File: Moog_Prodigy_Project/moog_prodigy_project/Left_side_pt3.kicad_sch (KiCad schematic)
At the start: 68 parts, among them J1 P2-3, J2 P2-4, J3 P2-2, J4 P2-1, J5 P2-1, SW6 Switch_1x3, SW7 Switch_4x4, SW8 SW_Slide_DPDT_3x3, U10 NE5532, U11 OPA234, U12 OPA134, U13 NE5532, U14 OPA134, U9 NE5532

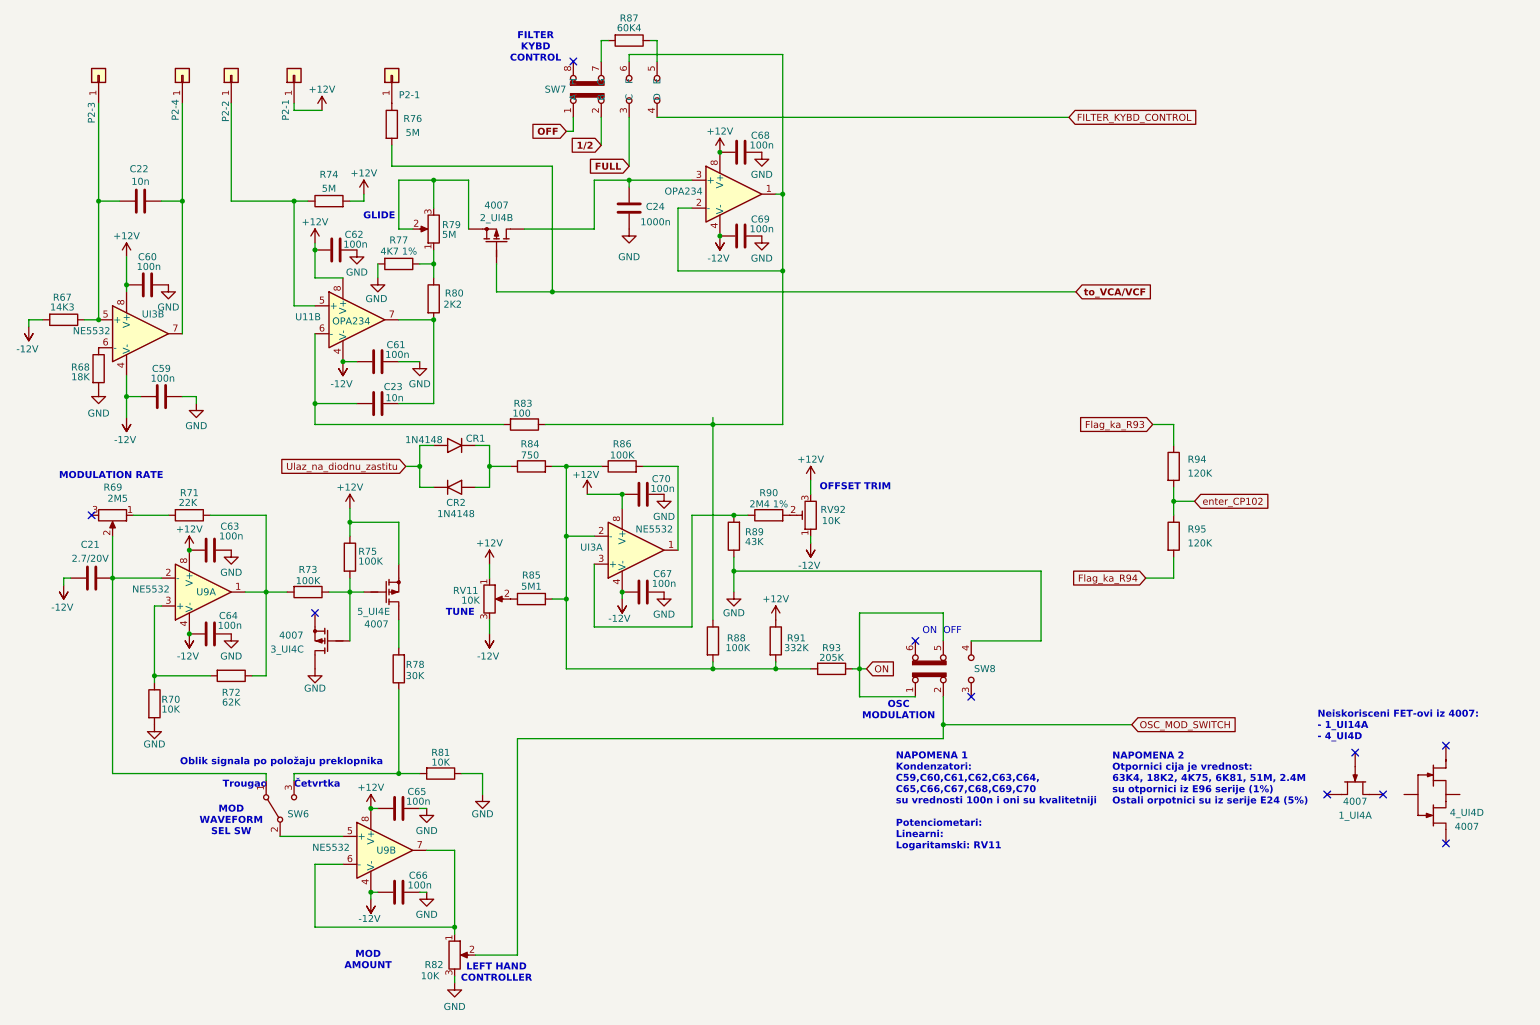
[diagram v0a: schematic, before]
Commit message: Moog prodigy fix 3
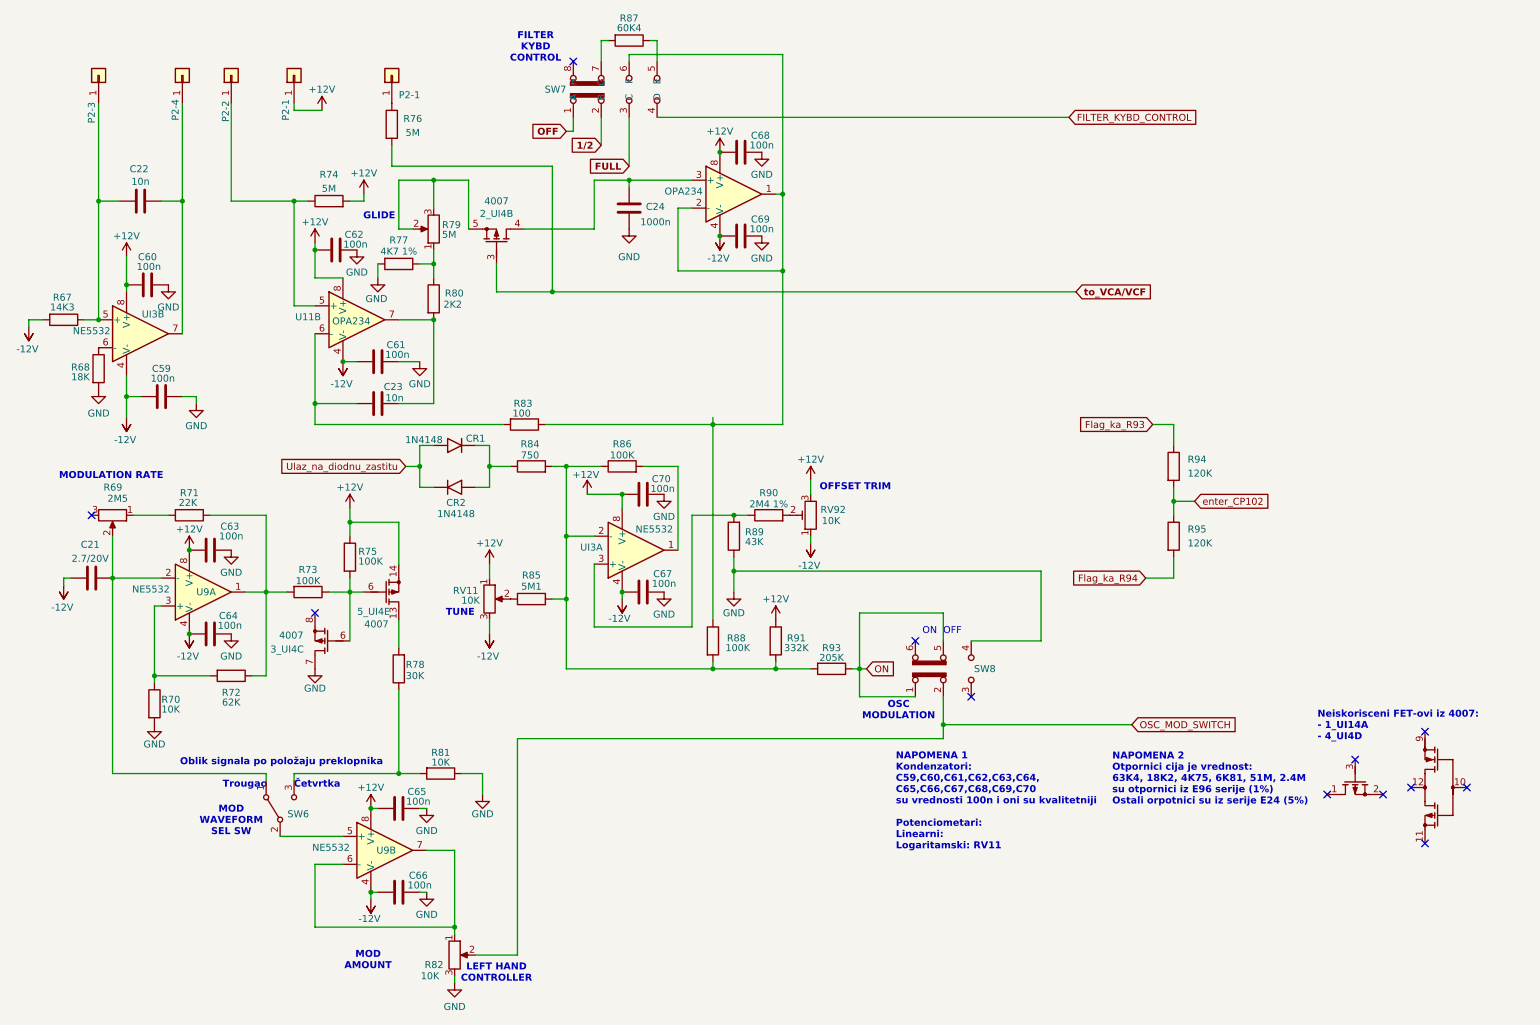
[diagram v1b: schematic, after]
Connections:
- net +12V: now also 5_UI4.14; no longer 5_UI4.
- net GND: now also 3_UI4.7; no longer 3_UI4.
- net to_VCA/VCF: now also 2_UI4.3; no longer 2_UI4.
- net at R73.1, R75.2: now also 3_UI4.6, 5_UI4.6; no longer 3_UI4., 5_UI4.
- net at C24.2, U11.3 (+): now also 2_UI4.4; no longer 2_UI4.
- net at R78.2: now also 5_UI4.13; no longer 5_UI4.
- net at R79.2, R79.3: now also 2_UI4.5; no longer 2_UI4.
- no-connect marks 10 -> 12
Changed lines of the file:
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@@
 	)
 	(no_connect
-		(at 276.86 163.83)
+		(at 273.05 163.83)
 	)
 	(no_connect
@@
 	)
 	(no_connect
-		(at 276.86 146.05)
+		(at 280.67 153.67)
+	)
+	(no_connect
+		(at 273.05 143.51)
 	)
 	(no_connect
@@
 	)
 	(no_connect
-		(at 260.35 147.32)
+		(at 260.35 148.59)
+	)
+	(no_connect
+		(at 270.51 153.67)
 	)
 	(wire
@@
 		(dnp no)
 		(property "Reference" "2_UI4"
-			(at 104.14 50.038 90)
+			(at 104.14 49.276 90)
 			(effects
 				(font
@@
 		)
 		(property "Value" "4007"
-			(at 104.14 47.752 90)
+			(at 104.14 46.99 90)
 			(effects
 				(font
@@
 		(pin ""
 		)
-		(pin ""
+		(pin "5"
 		)
 		(pin ""
 		)
-		(pin ""
+		(pin "3"
 		)
 		(pin ""
 		)
-		(pin ""
+		(pin "4"
 		)
 		(instances
@@
 		(pin ""
 		)
-		(pin ""
+		(pin "6"
 		)
 		(pin ""
@@
 		(pin ""
 		)
-		(pin ""
+		(pin "8"
 		)
 		(pin ""
 		)
-		(pin ""
+		(pin "7"
 		)
 		(pin ""
@@
 		(lib_name "4007_Novi_1")
 		(lib_id "Transistor_FET:4007_Novi")
-		(at 260.35 154.94 90)
+		(at 260.35 163.83 90)
 		(unit 1)
 		(exclude_from_sim no)
@@
 		(fields_autoplaced yes)
 		(property "Reference" "1_UI4"
-			(at 260.35 158.75 90)
+			(at 260.35 167.64 90)
 			(effects
 				(font
 					(size 1.27 1.27)
 				)
+				(hide yes)
 			)
 		)
 		(property "Value" "4007"
-			(at 260.35 156.21 90)
+			(at 260.35 165.1 90)
 			(effects
 				(font
 					(size 1.27 1.27)
 				)
+				(hide yes)
 			)
 		)
 		(property "Footprint" "Package_DIP:DIP-14_W7.62mm_Socket"
-			(at 260.35 154.94 0)
+			(at 260.35 163.83 0)
 			(effects
 				(font
@@
 		)
 		(property "Datasheet" ""
-			(at 260.35 154.94 0)
+			(at 260.35 163.83 0)
 			(effects
 				(font
@@
 		)
 		(property "Description" ""
-			(at 260.35 154.94 0)
+			(at 260.35 163.83 0)
 			(effects
 				(font
@@
 		(pin ""
 		)
-		(pin ""
+		(pin "3"
 		)
-		(pin ""
+		(pin "2"
 		)
-		(pin ""
+		(pin "1"
 		)
 		(pin ""
@@
 		(pin ""
 		)
-		(pin ""
+		(pin "14"
 		)
 		(pin ""
@@
 		(pin ""
 		)
-		(pin ""
+		(pin "13"
 		)
 		(pin ""
@@
 		(pin ""
 		)
-		(pin ""
+		(pin "6"
 		)
 		(pin ""
@@
 		(lib_name "4007_Novi_2")
 		(lib_id "Transistor_FET:4007_Novi")
-		(at 276.86 158.75 180)
+		(at 274.32 156.21 180)
 		(unit 4)
 		(exclude_from_sim no)
@@
 		(dnp no)
 		(property "Reference" "4_UI4"
-			(at 280.67 158.242 0)
+			(at 281.686 157.734 0)
 			(effects
 				(font
 					(size 1.27 1.27)
 				)
+				(hide yes)
 			)
 		)
 		(property "Value" "4007"
-			(at 280.67 160.782 0)
+			(at 278.13 158.242 0)
 			(effects
 				(font
 					(size 1.27 1.27)
 				)
+				(hide yes)
 			)
 		)
 		(property "Footprint" "Package_DIP:DIP-14_W7.62mm_Socket"
-			(at 276.86 158.75 0)
+			(at 280.67 153.67 0)
 			(effects
 				(font
@@
 		)
 		(property "Datasheet" ""
-			(at 276.86 158.75 0)
+			(at 274.32 156.21 0)
 			(effects
 				(font
@@
 		)
 		(property "Description" ""
-			(at 276.86 158.75 0)
+			(at 274.32 156.21 0)
 			(effects
 				(font
@@
 		(pin ""
 		)
-		(pin ""
+		(pin "10"
 		)
 		(pin ""
@@
 		(pin ""
 		)
-		(pin ""
+		(pin "11"
 		)
-		(pin ""
+		(pin "9"
 		)
-		(pin ""
+		(pin "12"
 		)
 		(instances

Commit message: treba mi da preraspodelim CA 3046
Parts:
- 2_UI4, 3_UI4, 5_UI4: value 4007 -> MC14007UBCP
- renumbered CR2 to D8, CR1 to D9
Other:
- note added: "Neiskorisceni FET-ovi iz MC14007UBCP - 1_UI14A - 4_UI4D"
- note removed: "Neiskorisceni FET-ovi iz 4007: - 1_UI14A - 4_UI4D"
- moved on the sheet: C60, R78

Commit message: 04.07.2026 Dodati tolerancije, E94, prosiriti spisak
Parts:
- U10: value NE5532 -> ~
- UI3: footprint NE5532AP:DIP794W45P254L1016H508Q8 -> Package_DIP:DIP-8_W7.62mm
- renumbered RV11 to RV11_LOG
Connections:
- net Flag_ka_R93 renamed Flag_to_R93
- net Flag_ka_R94 renamed Flag_to_R94
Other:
- note added: "32-key keyboard matrix generating scaled control voltages for VCO and filter tracking"
- note added: "NAPOMENA 1 Kondenzatori: C59,C60,C61,C62,C63,C64, C65,C66,C67,C68,C69,C70 su vrednosti 100n i oni su kvalitetniji"
- note added: "Not used FETs from MC14007UBCP - 1_UI14A - 4_UI4D"
- note added: "SIGNAL SHAPE TRIANGLE SQUARE"
- note removed: "NAPOMENA 1 Kondenzatori: C59,C60,C61,C62,C63,C64, C65,C66,C67,C68,C69,C70 su vrednosti 100n i oni su kvalitetniji Potenciometari: Linearni: Logaritamski: RV11"
- note removed: "Neiskorisceni FET-ovi iz MC14007UBCP - 1_UI14A - 4_UI4D"
- note removed: "Oblik signala po položaju preklopnika Trougao Četvrtka"
- moved on the sheet: 2_UI4B, 3_UI4C, C59, C63, C64, R75, R78, R83, R85, R86, R89, R90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

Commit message: 07.06.2026 fix 3
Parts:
- added R121, R122, R124, R125, R140: 2K, Resistor_THT:R_Axial_DIN0207_L6.3mm_D2.5mm_P7.62mm_Horizontal, symbol Device:R
- added R123: 100, Resistor_THT:R_Axial_DIN0207_L6.3mm_D2.5mm_P7.62mm_Horizontal, symbol Device:R
- R68: value 18K -> 17K8
- R71: value 22K -> 20K
- R72: value 62K -> 61K9
- R74, R79: value 5M -> 5M1
- R77: value 4K7 1% -> 4K75 1%
- R78: value 30K -> 28K
- R89: value 43K -> 43K2
- R90: value 2M4 1% -> 2M43
- R94, R95: value 120K -> 118K
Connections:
- net Flag_to_R94: now also R140.2; no longer R95.2
- net GND: now also R121.2; no longer R68.2
- net enter_CP102: now also R125.2; no longer R94.2
- net at R73.2, U9.1: now also R122.1, R123.1; no longer R71.1, R72.1
- net at R84.2, R85.2, R86.1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: now also UI3.3 (+); no longer UI3.2 (-)
- net at R81.2, SW6.3 (C): now also R124.1; no longer R78.1
- net at R89.2, R90.1: now also UI3.2 (-); no longer UI3.3 (+)
- net at C21.1, R69.2, SW6.1 (A): now also U9.3 (+); no longer U9.2 (-)
- net at R70.1, R72.2: now also U9.2 (-); no longer U9.3 (+)
- new net: R125.1, R94.2
- new net: R140.1, R95.2
- new net: R122.2, R71.1
- new net: R121.1, R68.2
- new net: R123.2, R72.1
- new net: R124.2, R78.1
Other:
- note removed: "NAPOMENA 2 Otpornici cija je vrednost: 63K4, 18K2, 4K75, 6K81, 51M, 2.4M su otpornici iz E96 serije (1%) Ostali orpotnici su iz serije E24 (5%)"
- moved on the sheet: R71, R72, R78, R85, R94, R95, RV11_LOG

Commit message: CA3046 nova schema
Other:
- note added: "NAPOMENA 1 Kondenzatori: C21,C24,C59,C60,C61,C62,C63,C64, C65,C66,C67,C68,C69,C70 su vrednosti 100n i oni su kvalitetniji"
- note removed: "NAPOMENA 1 Kondenzatori: C59,C60,C61,C62,C63,C64, C65,C66,C67,C68,C69,C70 su vrednosti 100n i oni su kvalitetniji"
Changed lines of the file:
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@@
 		)
 	)
-	(text "NAPOMENA 1\nKondenzatori:\nC59,C60,C61,C62,C63,C64,\nC65,C66,C67,C68,C69,C70\nsu vrednosti 100n i oni su kvalitetniji"
+	(text "NAPOMENA 1\nKondenzatori:\nC21,C24,C59,C60,C61,C62,C63,C64,\nC65,C66,C67,C68,C69,C70\nsu vrednosti 100n i oni su kvalitetniji"
 		(exclude_from_sim no)
 		(at 176.784 156.21 0)

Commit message: 08.07.2026 fix
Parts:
- removed C24: 1000n, Capacitor_THT:C_Disc_D3.8mm_W2.6mm_P2.50mm, symbol Device:C
- removed R121, R122, R124, R125, R140: 2K, Resistor_THT:R_Axial_DIN0207_L6.3mm_D2.5mm_P7.62mm_Horizontal, symbol Device:R
- removed R123: 100, Resistor_THT:R_Axial_DIN0207_L6.3mm_D2.5mm_P7.62mm_Horizontal, symbol Device:R
- added C24: 1u/25V, Capacitor_THT:CP_Radial_D5.0mm_P2.50mm, symbol elektrolitski:elektrolit
- C21: value 2.7/20V -> 2u7/25V
- R68: value 17K8 -> 18K 5%
- R71: value 20K -> 22K 10%
- R72: value 61K9 -> 62K 5%
- R78: value 28K -> 30K 5%
- R84: value 750 -> 750K
- R94, R95: value 118K -> 120K 5%
- RV11: renamed from RV11_LOG; value 10K -> 10K LOG
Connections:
- net enter_CP102 is gone; now on net Input to C39: R95.1
- net GND: now also R68.2, C24.
- net Input to C39: now reaches R94.2
- net Flag to R94: now reaches R95.2
- net at R71.1: now also R72.1, R73.2, U9.1
- net at 2_UI4.4, U11.3 (+): now also C24.
- net at R78.1: now also R81.2, SW6.3 (C)
- net Flag to R87: now reaches R86.2, UI3.1
- net 1/2: no longer names the net of SW7.2
- net FILTER_KYBD_CONTROL renamed FILTER KYBD CONTROL
- net FULL: no longer names the net of SW7.3
- net OFF: no longer names the net of SW7.1
- net OSC_MOD_SWITCH renamed OSC MOD SWITCH
- net Ulaz_na_diodnu_zastitu renamed Input to diode protection
- net to_VCA/VCF renamed Input to VCA/VCF
- no-connect marks 12 -> 15
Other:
- note added: "OFF 1/2 FULL"
- note added: "PP"
- note removed: "NAPOMENA 1 Kondenzatori: C21,C24,C59,C60,C61,C62,C63,C64, C65,C66,C67,C68,C69,C70 su vrednosti 100n i oni su kvalitetniji"
- moved on the sheet: C22, C60, R68, R71, R72, R78, R83, R84, R85, R95, RV11

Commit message: Finalni deo seme, prelaz na PCB
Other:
- note added: "*GENERAL NOTE* Resistor values that are not explicitly specified are selected from the E96 value series with a tolerance of ±1%."
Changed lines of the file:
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@@
 		)
 	)
+	(text "*GENERAL NOTE*\nResistor values that are not explicitly specified\nare selected from the E96 value series with a \ntolerance of ±1%."
+		(exclude_from_sim no)
+		(at 176.784 161.036 0)
+		(effects
+			(font
+				(size 1.27 1.27)
+				(thickness 0.254)
+				(bold yes)
+			)
+			(justify left)
+		)
+	)
 	(text "ON  OFF "
 		(exclude_from_sim no)
@@
 	)
 	(symbol
+		(lib_name "elektrolit_1")
+		(lib_id "elektrolitski:elektrolit")
+		(at 132.08 46.99 0)
+		(unit 1)
+		(exclude_from_sim no)
+		(in_bom yes)
+		(on_board yes)
+		(dnp no)
+		(property "Reference" "C24"
+			(at 128.778 46.99 0)
+			(effects
+				(font
+					(size 1.27 1.27)
+				)
+				(justify right)
+			)
+		)
+		(property "Value" "1u/25V"
+			(at 131.826 49.53 0)
+			(effects
+				(font
+					(size 1.27 1.27)
+				)
+				(justify right)
+			)
+		)
+		(property "Footprint" "Capacitor_THT:CP_Radial_D5.0mm_P2.50mm"
+			(at 132.08 58.42 0)
+			(effects
+				(font
+					(size 1.27 1.27)
+				)
+				(hide yes)
+			)
+		)
+		(property "Datasheet" ""
+			(at 131.826 46.99 0)
+			(effects
+				(font
+					(size 1.27 1.27)
+				)
+				(hide yes)
+			)
+		)
+		(property "Description" ""
+			(at 132.08 46.99 0)
+			(effects
+				(font
+					(size 1.27 1.27)
+				)
+			)
+		)
+		(property "Rated Voltage" "25V"
+			(at 128.524 51.308 0)
+			(effects
+				(font
+					(size 1.27 1.27)
+				)
+				(hide yes)
+			)
+		)
+		(pin ""
+		)
+		(pin ""
+		)
+		(instances
+			(project "moog_prodigy_project"
+				(path "/db469bdb-b6c3-4a16-9199-d4e6b8d556e8/e17106b4-4b3e-4539-a6cd-812d9801e405"
+					(reference "C24")
+					(unit 1)
+				)
+			)
+		)
+	)
+	(symbol
 		(lib_id "Device:R")
 		(at 165.1 132.08 270)
@@
 				)
 			)
-		)
-	)
-	(symbol
-		(lib_name "elektrolit_1")
-		(lib_id "elektrolitski:elektrolit")
-		(at 132.08 46.99 0)
-		(unit 1)
-		(exclude_from_sim no)
-		(in_bom yes)
-		(on_board yes)
-		(dnp no)
-		(property "Reference" "C24"
-			(at 128.778 46.99 0)
-			(effects
-				(font
-					(size 1.27 1.27)
-				)
-				(justify right)
-			)
-		)
-		(property "Value" "1u/25V"
-			(at 131.826 49.53 0)
-			(effects
-				(font
-					(size 1.27 1.27)
-				)
-				(justify right)
-			)
-		)
-		(property "Footprint" "Capacitor_THT:CP_Radial_D5.0mm_P2.50mm"
-			(at 132.08 58.42 0)
-			(effects
-				(font
-					(size 1.27 1.27)
-				)
-				(hide yes)
-			)
-		)
-		(property "Datasheet" ""
-			(at 131.826 46.99 0)
-			(effects
-				(font
-					(size 1.27 1.27)
-				)
-				(hide yes)
-			)
-		)
-		(property "Description" ""
-			(at 132.08 46.99 0)
-			(effects
-				(font
-					(size 1.27 1.27)
-				)
-			)
-		)
-		(property "Rated Voltage" "25V"
-			(at 128.524 51.308 0)
-			(effects
-				(font
-					(size 1.27 1.27)
-				)
-				(hide yes)
-			)
-		)
-		(pin ""
-		)
-		(pin ""
-		)
-		(instances
-			(project "moog_prodigy_project"
-				(path "/db469bdb-b6c3-4a16-9199-d4e6b8d556e8/e17106b4-4b3e-4539-a6cd-812d9801e405"
-					(reference "C24")
-					(unit 1)
-				)
-			)

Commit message: Update tracks 16.07.2026
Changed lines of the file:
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@@
 		)
 		(property "Value" "NE5532"
-			(at 64.516 166.624 0)
+			(at 64.77 165.862 0)
 			(effects
 				(font
@@
 				)
 				(justify left)
-			)
-		)
+				(hide yes)
+			)
+		)
